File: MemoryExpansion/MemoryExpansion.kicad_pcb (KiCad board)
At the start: 4 copper layers, 71.2 x 55.2 mm, 9 parts, among them J1 1.5MB RAM Expansion, U1 74LS139, U2 AS6C4008-55PCN, U3 AS6C4008-55PCN, U4 AS6C4008-55PCN

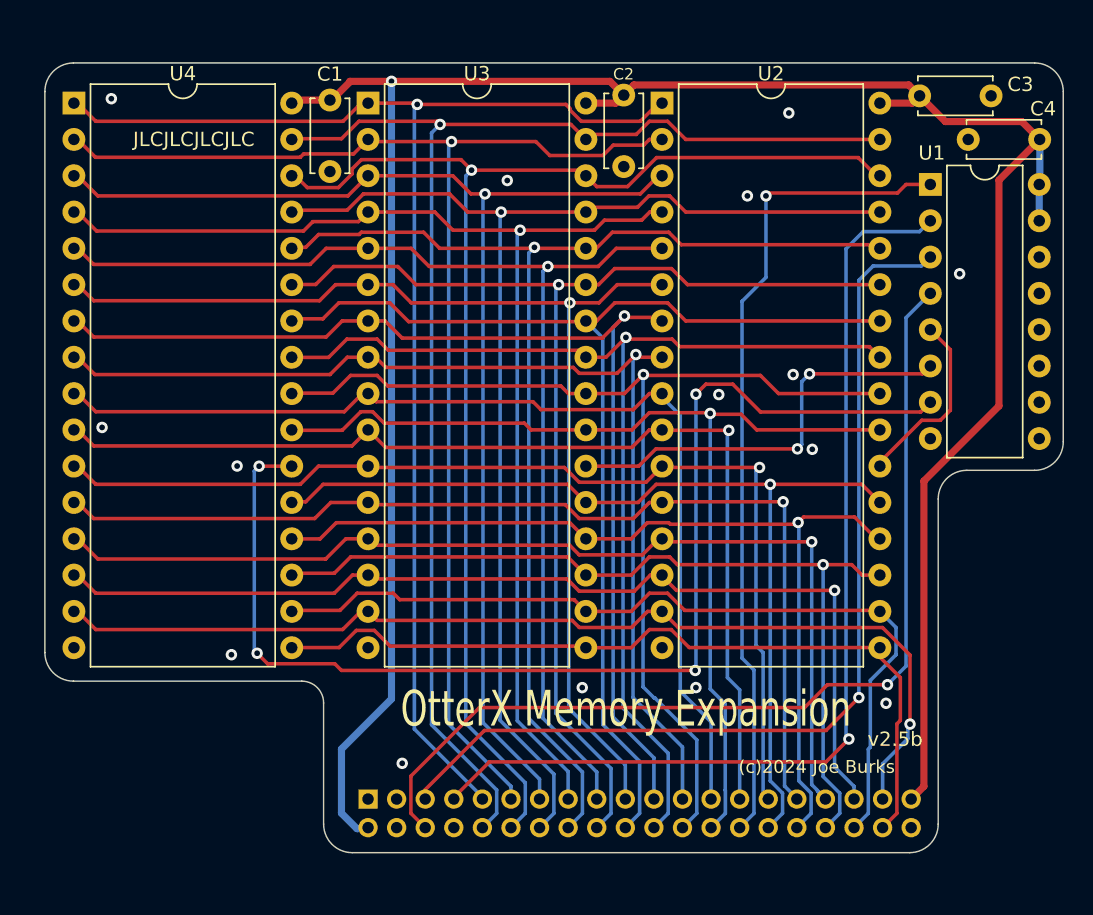
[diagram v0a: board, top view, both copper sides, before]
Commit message: Change 2.2u cap footprint; update MemoryExpansion
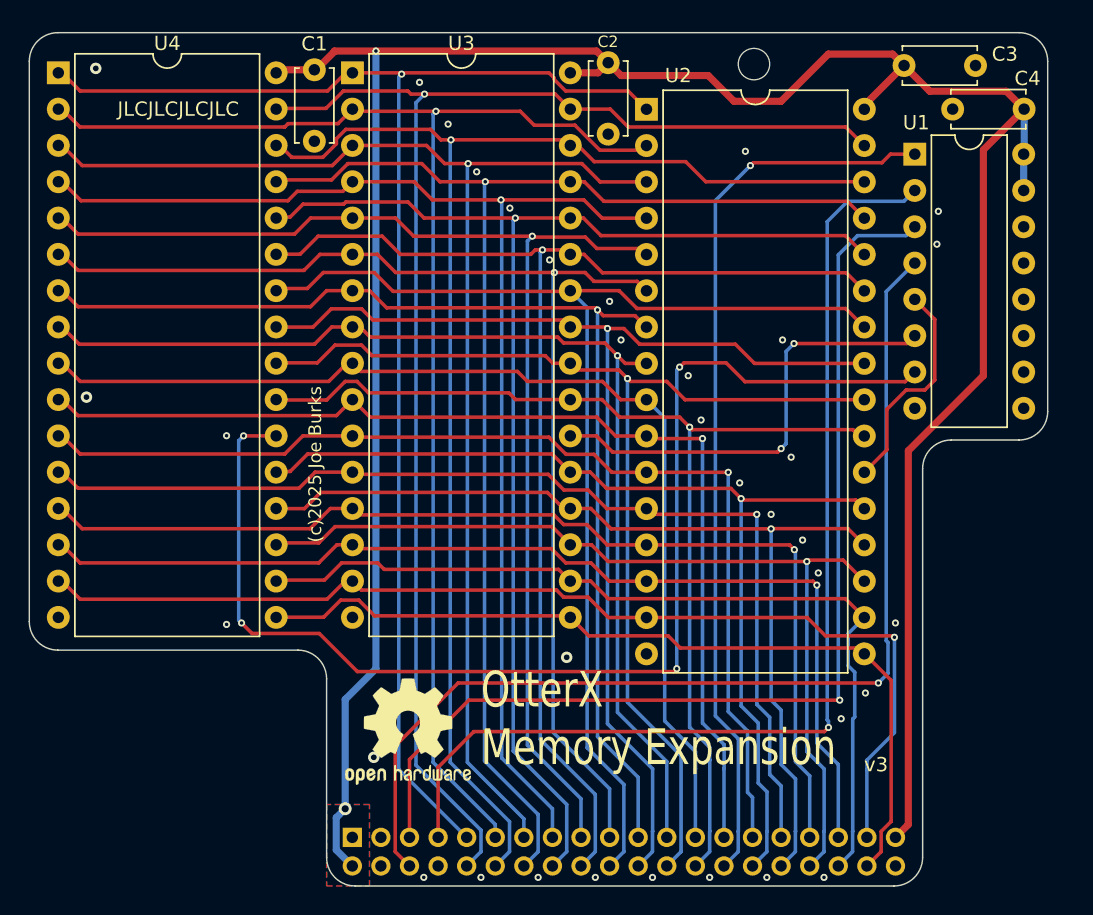
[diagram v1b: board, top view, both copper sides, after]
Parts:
- added H1: MountingHole, MountingHole:MountingHole_2.2mm_M2, F.Cu at (141.5, 42.4)
- added REF**: OSHW-Logo2_9.8x8mm_SilkScreen, Symbol:OSHW-Logo2_9.8x8mm_SilkScreen, F.Cu at (117.3, 89.1)
- moved J1 2.90 mm to (113.4, 96.5)
- moved C2 2.52 mm to (131.3, 42.3)
- moved C4 2.38 mm to (160.4, 45.5)
- moved U3 2.38 mm to (113.4, 43.0)
- moved U4 2.38 mm to (92.8, 43.0)
- moved C1 2.38 mm to (110.7, 42.8)
- moved C3 2.38 mm to (152.0, 42.5)
- moved U1 2.38 mm to (152.8, 48.7)
- moved U2 1.17 mm to (134.0, 45.6)
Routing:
- net +5V: track 171.0 -> 182.9 mm, vias 1 -> 2
- net ~{BRAMEN0}: track 68.6 -> 75.0 mm
- net /BA20: track 68.5 -> 74.6 mm
- net /A8: track 82.7 -> 88.4 mm
- net ~{WE}: track 86.9 -> 92.5 mm
- net /BA15: track 93.9 -> 99.5 mm
- net ~{BRAMEN}: track 57.5 -> 62.9 mm
- net /BA16: track 90.3 -> 95.7 mm
- net /BA19: track 70.4 -> 75.8 mm
- net /BA13: track 84.8 -> 90.1 mm
- net /BA18: track 92.8 -> 98.1 mm
- net /A9: track 79.9 -> 85.0 mm
- net /A6: track 79.0 -> 84.1 mm
- net /BA14: track 86.9 -> 91.9 mm
- net /A12: track 84.2 -> 89.1 mm
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- added copper zone on B.Cu, net +5V
- added copper zone on F.Cu, net +5V
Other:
- board size 71.2 x 55.2 mm -> 71.3 x 59.7 mm
- board text added: "(c)2025 Joe Burks"
- board text added: "v3"
- board text removed: "(c)2024 Joe Burks"
- board text removed: "v2.5b"
